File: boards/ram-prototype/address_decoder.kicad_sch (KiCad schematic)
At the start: 33 parts, among them U1 74LVC1G04, U10 74LVC1G11, U11 74LVC1G11, U2 74LVC1G04, U3 74LVC1G04, U4 74LVC1G11, U5 74LVC1G11, U6 74LVC1G11, U7 74LVC1G11, U8 74LVC1G11, U9 74LVC1G11

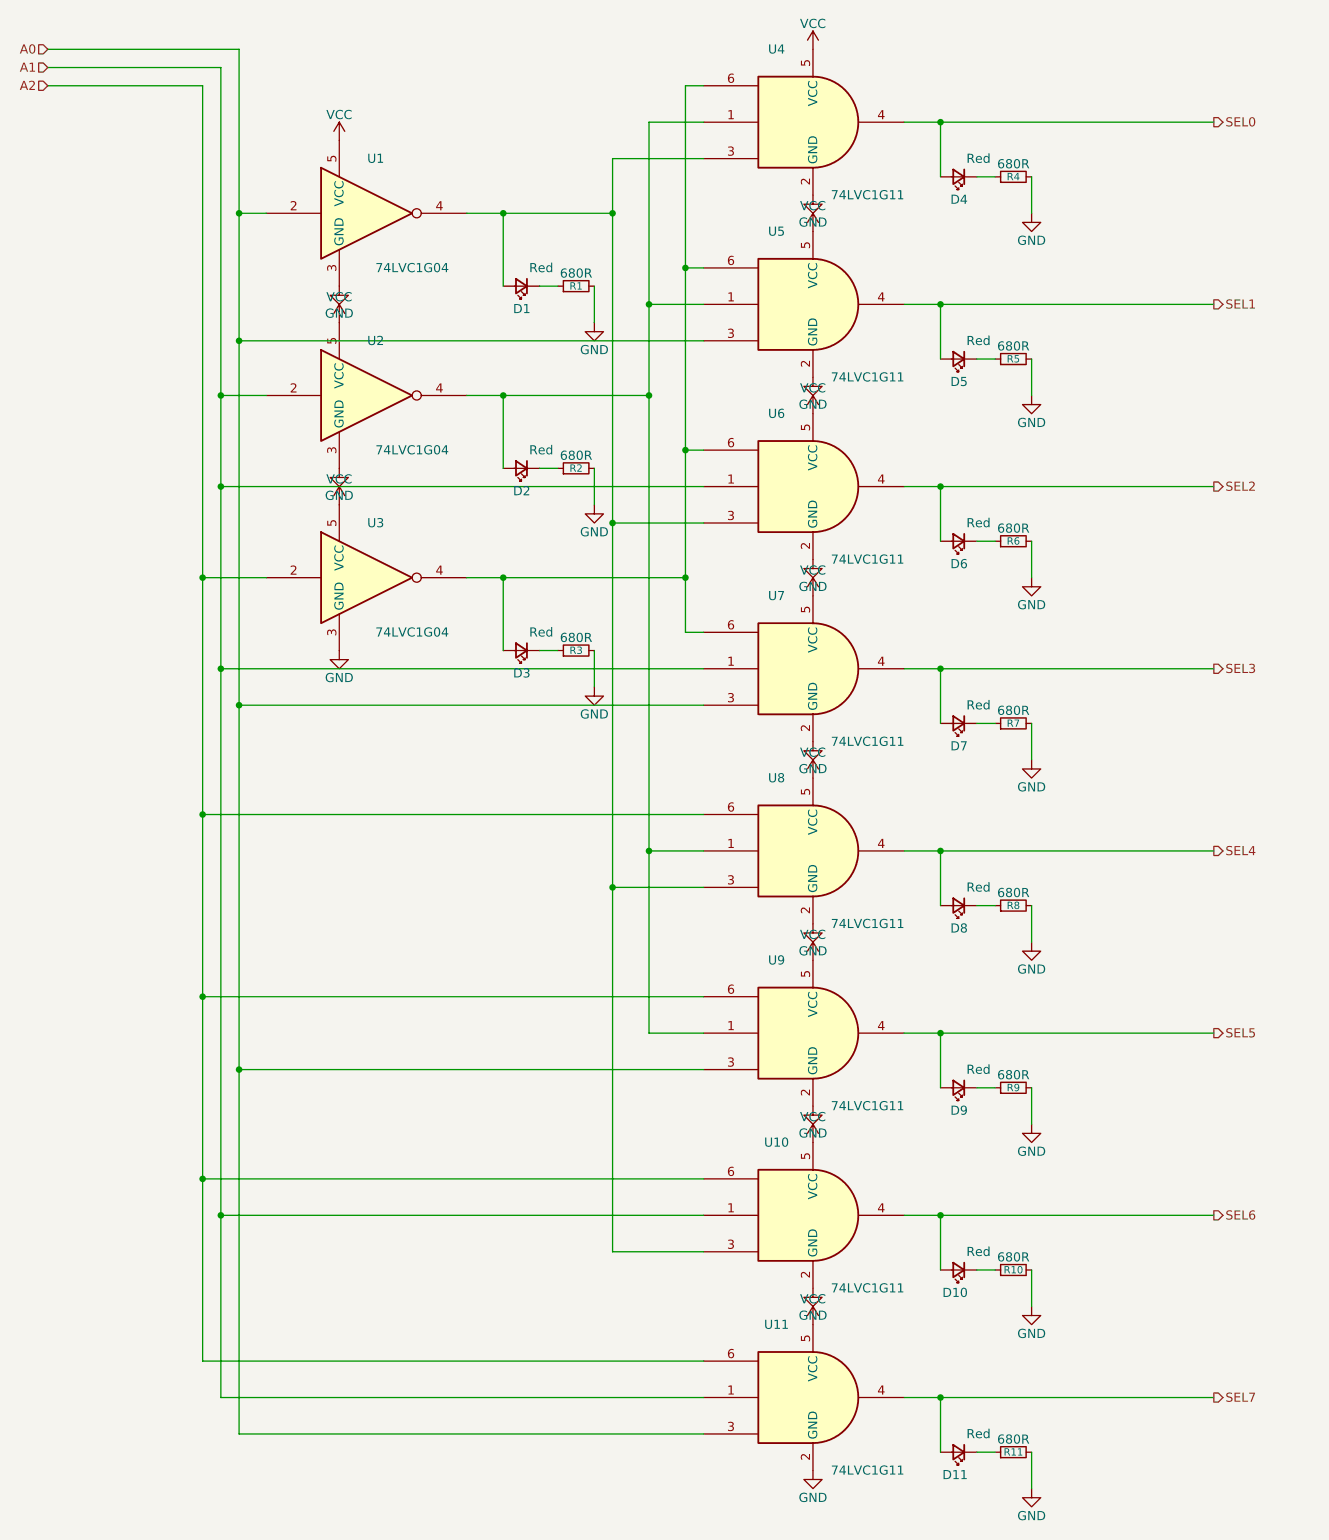
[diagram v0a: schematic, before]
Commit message: Update schematic with new row/col architecture
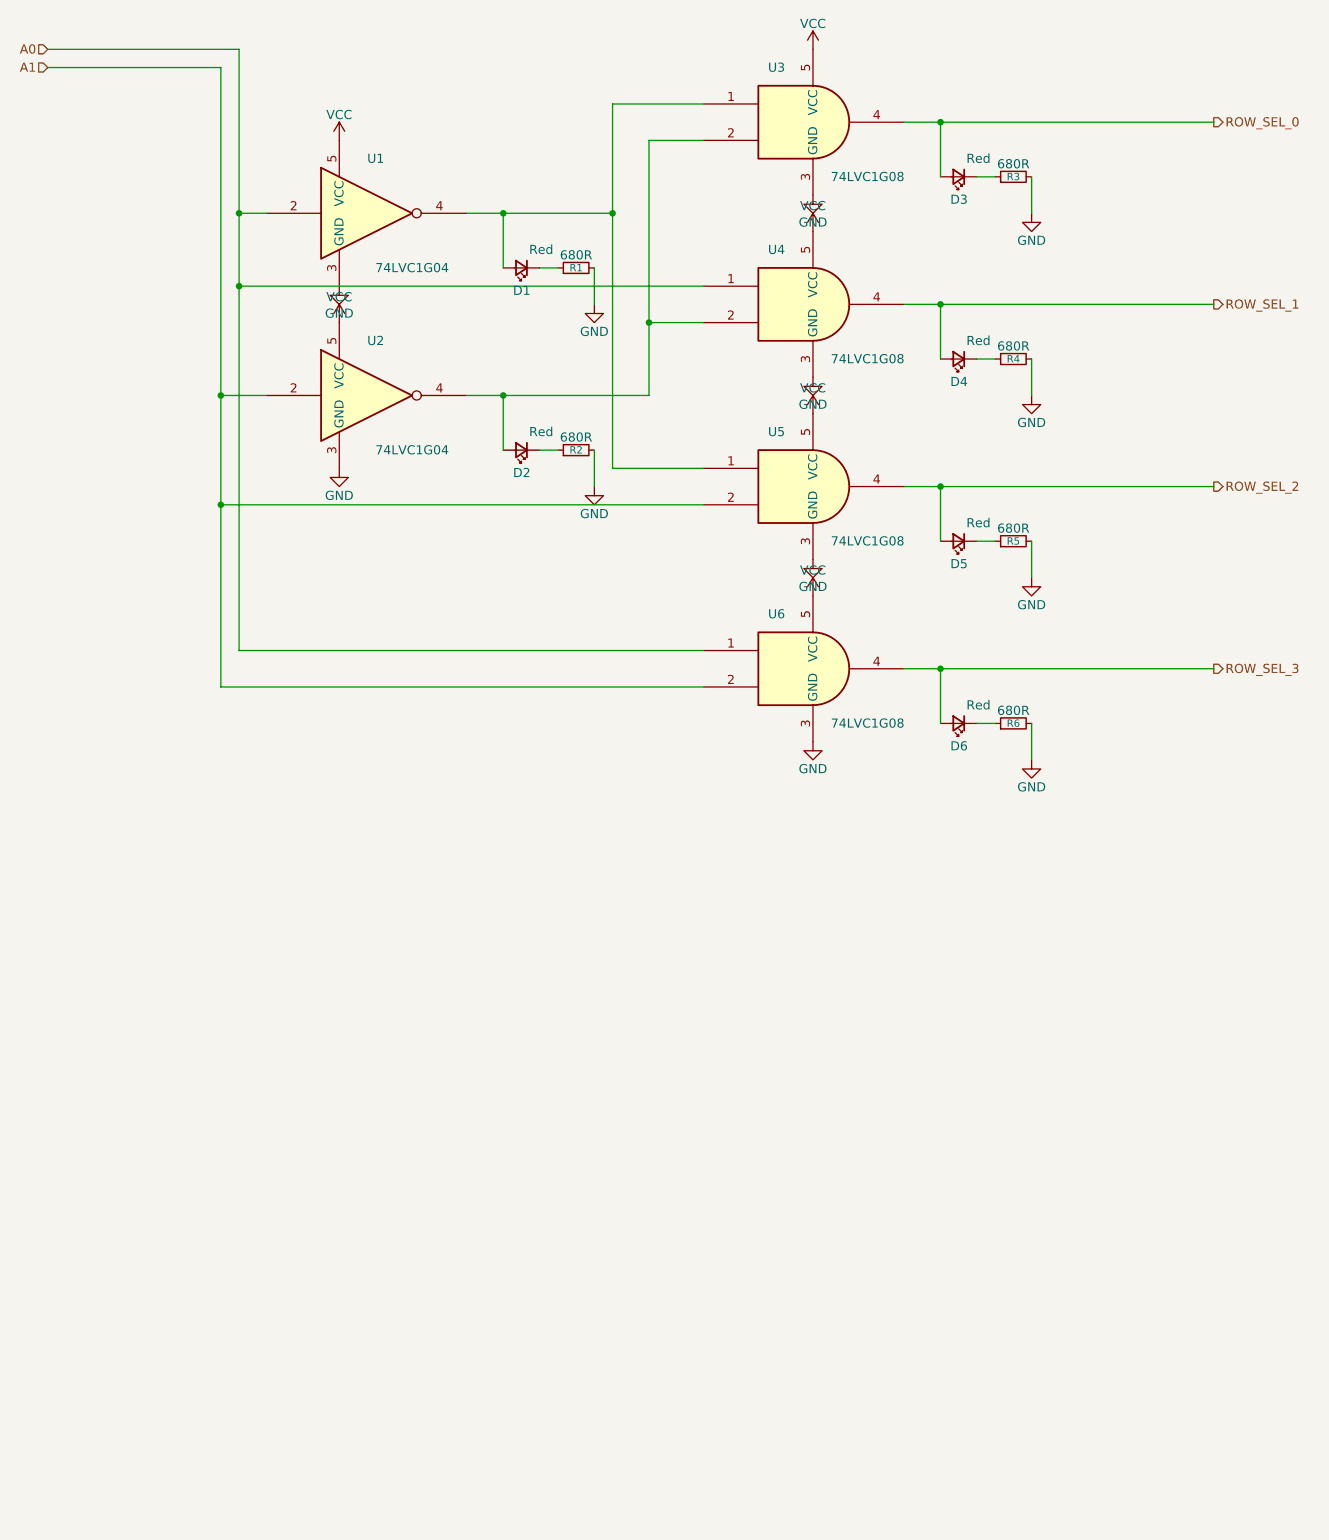
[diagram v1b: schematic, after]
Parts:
- removed D10, D11, D7, D8, D9: Red, symbol Device:LED_Small
- removed R10, R11, R7, R8, R9: 680R, symbol Device:R_Small
- removed U10, U11, U4, U5, U6, U7, U8, U9: 74LVC1G11, symbol 74xGxx:74LVC1G11
- removed U3: 74LVC1G04, symbol 74xGxx:74LVC1G04
- added U3, U4, U5, U6: 74LVC1G08, symbol 74xGxx:74LVC1G08
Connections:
- net A0: now also U4.1, U6.1
- net A1: now also U5.2, U6.2
- net GND: now also U3.3 (GND), U4.3 (GND), U5.3 (GND), U6.3 (GND)
- net VCC: now also U3.5 (VCC), U4.5 (VCC), U5.5 (VCC), U6.5 (VCC)
- net at D2.2 (A), U2.4: now also U3.2, U4.2
- net at D1.2 (A), U1.4: now also U3.1, U5.1
- net ROW_SEL_0: now reaches D3.2 (A)
- net ROW_SEL_0: now also U3.4
- net SEL0 renamed ROW_SEL_1
- net ROW_SEL_1: now also U4.4
- net SEL1 renamed ROW_SEL_2
- net ROW_SEL_2: now also U5.4
- net SEL2 renamed ROW_SEL_3
- net ROW_SEL_3: now also U6.4

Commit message: Add initial changes to make logic close to final
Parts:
- removed U3, U4, U5, U6: 74LVC1G08, symbol 74xGxx:74LVC1G08
- added D10, D11, D12, D13, D14, D15, D16, D17, D18, D19, D7, D8, D9: Red, symbol Device:LED_Small
- added R10, R11, R12, R13, R14, R15, R16, R17, R18, R19, R7, R8, R9: 680R, symbol Device:R_Small
- added U10, U11, U12, U13, U14, U15, U16, U17, U18, U19, U8, U9: 74LVC1G08, symbol 74xGxx:74LVC1G08
- added U3, U4, U5, U6, U7: 74LVC1G04, symbol 74xGxx:74LVC1G04
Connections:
- net A0: now also U13.2, U15.2
- net A1: now also U14.1, U15.1
- net GND: now also R10.2, R11.2, R12.2, R13.2, R14.2, R15.2, R16.2, R17.2, R18.2, R19.2, R7.2, R8.2, R9.2, U10.3 (GND), U11.3 (GND), U12.3 (GND), U13.3 (GND), U14.3 (GND), U15.3 (GND), U16.3 (GND), U17.3 (GND), U18.3 (GND), U19.3 (GND), U3.3 (GND), U4.3 (GND), U5.3 (GND), U6.3 (GND), U7.3 (GND), U8.3 (GND), U9.3 (GND)
- net ROW_SEL_0: now also D16.2 (A), U16.4; no longer D3.2 (A)
- net ROW_SEL_1: now also D17.2 (A), U17.4; no longer D4.2 (A)
- net ROW_SEL_2: now also D18.2 (A), U18.4; no longer D5.2 (A)
- net ROW_SEL_3: now also D19.2 (A), U19.4; no longer D6.2 (A)
- net VCC: now also U10.5 (VCC), U11.5 (VCC), U12.5 (VCC), U13.5 (VCC), U14.5 (VCC), U15.5 (VCC), U16.5 (VCC), U17.5 (VCC), U18.5 (VCC), U19.5 (VCC), U3.5 (VCC), U4.5 (VCC), U5.5 (VCC), U6.5 (VCC), U7.5 (VCC), U8.5 (VCC), U9.5 (VCC)
- net at D1.2 (A), U1.4: now also U12.2, U14.2
- net at D2.2 (A), U2.4: now also U12.1, U13.1
- new net: D9.1 (K), R9.1
- new net: D15.1 (K), R15.1
- new net: D15.2 (A), U15.4, U19.2
- new net: D10.1 (K), R10.1
- new net: D7.1 (K), R7.1
- new net: D14.2 (A), U14.4, U18.2
- new net: D6.2 (A), U6.4, U9.2
- new net: D18.1 (K), R18.1
- new net: D12.2 (A), U12.4, U16.2
- new net: D7.2 (A), U11.2, U7.4
- new net: D4.2 (A), U4.4, U8.2
- new net: D14.1 (K), R14.1
- new net: D8.1 (K), R8.1
- new net: D5.2 (A), U5.4, U9.1
- new net: D16.1 (K), R16.1
- new net: D12.1 (K), R12.1
- new net: D13.1 (K), R13.1
- new net: D13.2 (A), U13.4, U17.2
- new net: D19.1 (K), R19.1
- new net: D11.1 (K), R11.1
- new net: D3.2 (A), U3.4, U8.1
- new net: D17.1 (K), R17.1
- new net A2: U3.2
- new net A3: U4.2
- new net A4: U5.2
- new net A5: U6.2
- new net A6: U7.2
- new net RS1: D8.2 (A), U10.1, U8.4
- new net RS2: D9.2 (A), U10.2, U9.4
- new net RS3: D10.2 (A), U10.4, U11.1
- new net RS4: D11.2 (A), U11.4, U16.1, U17.1, U18.1, U19.1

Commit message: Update row select to have the full complexity to test latency
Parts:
- added D20, D21, D22, D23, D24, D25, D26, D27, D28, D29, D30, D31, D32, D33, D34, D35, D36, D37, D38, D39, D40, D41, D42, D43, D44, D45, D46, D47: Red, symbol Device:LED_Small
- added R20, R21, R22, R23, R24, R25, R26, R27, R28, R29, R30, R31, R32, R33, R34, R35, R36, R37, R38, R39, R40, R41, R42, R43, R44, R45, R46, R47: 680R, symbol Device:R_Small
- added U20, U21, U22, U23, U24, U25, U26, U27, U28, U29, U30, U31, U32, U33, U34, U35, U36, U37, U38, U39, U40, U41, U42, U43, U44, U45, U46, U47: 74LVC1G08, symbol 74xGxx:74LVC1G08
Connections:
- net A0: now also U17.2, U19.2
- net A1: now also U11.2, U9.2; no longer U14.1, U15.1
- net A2: now also U10.1, U11.1
- net A3: now also U21.2, U23.2
- net A4: now also U22.1, U23.1
- net A5: now also U25.2, U27.2
- net A6: now also U26.1, U27.1
- net GND: now also R20.2, R21.2, R22.2, R23.2, R24.2, R25.2, R26.2, R27.2, R28.2, R29.2, R30.2, R31.2, R32.2, R33.2, R34.2, R35.2, R36.2, R37.2, R38.2, R39.2, R40.2, R41.2, R42.2, R43.2, R44.2, R45.2, R46.2, R47.2, U20.3 (GND), U21.3 (GND), U22.3 (GND), U23.3 (GND), U24.3 (GND), U25.3 (GND), U26.3 (GND), U27.3 (GND), U28.3 (GND), U29.3 (GND), U30.3 (GND), U31.3 (GND), U32.3 (GND), U33.3 (GND), U34.3 (GND), U35.3 (GND), U36.3 (GND), U37.3 (GND), U38.3 (GND), U39.3 (GND), U40.3 (GND), U41.3 (GND), U42.3 (GND), U43.3 (GND), U44.3 (GND), U45.3 (GND), U46.3 (GND), U47.3 (GND)
- net ROW_SEL_0: now also D44.2 (A), U44.4; no longer D16.2 (A), U16.4
- net ROW_SEL_1: now also D45.2 (A), U45.4; no longer D17.2 (A), U17.4
- net ROW_SEL_2: now also D46.2 (A), U46.4; no longer D18.2 (A), U18.4
- net ROW_SEL_3: now also D47.2 (A), U47.4; no longer D19.2 (A), U19.4
- net VCC: now also U20.5 (VCC), U21.5 (VCC), U22.5 (VCC), U23.5 (VCC), U24.5 (VCC), U25.5 (VCC), U26.5 (VCC), U27.5 (VCC), U28.5 (VCC), U29.5 (VCC), U30.5 (VCC), U31.5 (VCC), U32.5 (VCC), U33.5 (VCC), U34.5 (VCC), U35.5 (VCC), U36.5 (VCC), U37.5 (VCC), U38.5 (VCC), U39.5 (VCC), U40.5 (VCC), U41.5 (VCC), U42.5 (VCC), U43.5 (VCC), U44.5 (VCC), U45.5 (VCC), U46.5 (VCC), U47.5 (VCC)
- net nA3: now reaches D4.2 (A), U4.4
- net nA3: now also U20.2, U22.2; no longer U8.2
- net nA2: now reaches D3.2 (A), U3.4, U8.1
- net nA2: now also U9.1
- net G0: now reaches U12.1, U13.1
- net G0: now also D8.2 (A), U8.4; no longer D2.2 (A), U2.4
- net nA0: now reaches D1.2 (A), U1.4, U12.2, U14.2
- net nA0: now also U16.2, U18.2
- net DEC3_0: now reaches D12.2 (A), U12.4
- net DEC3_0: now also U44.1; no longer U16.2
- net nA4: now reaches D5.2 (A), U5.4
- net nA4: now also U20.1, U21.1; no longer U9.1
- net nA5: now reaches D6.2 (A), U6.4
- net nA5: now also U24.2, U26.2; no longer U9.2
- net DEC3_1: now reaches D13.2 (A), U13.4
- net DEC3_1: now also U45.1; no longer U17.2
- net DEC3_2: now reaches D14.2 (A), U14.4
- net DEC3_2: now also U46.1; no longer U18.2
- net nA6: now reaches D7.2 (A), U7.4
- net nA6: now also U24.1, U25.1; no longer U11.2
- net DEC3_3: now reaches D15.2 (A), U15.4
- net DEC3_3: now also U47.1; no longer U19.2
- removed net RS1: D8.2 (A), U10.1, U8.4
- net RS2 renamed G1
- net G1: now also U14.1, U15.1; no longer U10.2
- net RS3 renamed G2
- net G2: now also U16.1, U17.1; no longer U11.1
- net RS4 renamed G3
- net G3: no longer U16.1, U17.1
- new net: D24.1 (K), R24.1
- new net: D47.1 (K), R47.1
- new net: D33.1 (K), R33.1
- new net: D32.1 (K), R32.1
- new net: D44.1 (K), R44.1
- new net: D37.1 (K), R37.1
- new net: D29.1 (K), R29.1
- new net: D23.1 (K), R23.1
- new net: D26.1 (K), R26.1
- new net: D38.1 (K), R38.1
- new net: D45.1 (K), R45.1
- new net: D35.1 (K), R35.1
- new net: D39.1 (K), R39.1
- new net: D21.1 (K), R21.1
- new net: D27.1 (K), R27.1
- new net: D46.1 (K), R46.1
- new net: D42.1 (K), R42.1
- new net: D43.1 (K), R43.1
- new net: D36.1 (K), R36.1
- new net: D30.1 (K), R30.1
- new net: D41.1 (K), R41.1
- new net: D28.1 (K), R28.1
- new net: D20.1 (K), R20.1
- new net: D34.1 (K), R34.1
- new net: D22.1 (K), R22.1
- new net: D31.1 (K), R31.1
- new net: D25.1 (K), R25.1
- new net: D40.1 (K), R40.1
- new net DEC3_4: D16.2 (A), U16.4
- new net DEC3_5: D17.2 (A), U17.4
- new net DEC3_6: D18.2 (A), U18.4
- new net DEC3_7: D19.2 (A), U19.4
- new net DEC4_0: D28.2 (A), U28.4, U44.2, U45.2, U46.2, U47.2
- new net DEC4_1: D29.2 (A), U29.4
- new net DEC4_10: D38.2 (A), U38.4
- new net DEC4_11: D39.2 (A), U39.4
- new net DEC4_12: D40.2 (A), U40.4
- new net DEC4_13: D41.2 (A), U41.4
- new net DEC4_14: D42.2 (A), U42.4
- new net DEC4_15: D43.2 (A), U43.4
- new net DEC4_2: D30.2 (A), U30.4
- new net DEC4_3: D31.2 (A), U31.4
- new net DEC4_4: D32.2 (A), U32.4
- new net DEC4_5: D33.2 (A), U33.4
- new net DEC4_6: D34.2 (A), U34.4
- new net DEC4_7: D35.2 (A), U35.4
- new net DEC4_8: D36.2 (A), U36.4
- new net DEC4_9: D37.2 (A), U37.4
- new net HA0: D20.2 (A), U20.4, U28.2, U32.2, U36.2, U40.2
- new net HA1: D21.2 (A), U21.4, U29.2, U33.2, U37.2, U41.2
- new net HA2: D22.2 (A), U22.4, U30.2, U34.2, U38.2, U42.2
- new net HA3: D23.2 (A), U23.4, U31.2, U35.2, U39.2, U43.2
- new net HB0: D24.2 (A), U24.4, U28.1, U29.1, U30.1, U31.1
- new net HB1: D25.2 (A), U25.4, U32.1, U33.1, U34.1, U35.1
- new net HB2: D26.2 (A), U26.4, U36.1, U37.1, U38.1, U39.1
- new net HB3: D27.2 (A), U27.4, U40.1, U41.1, U42.1, U43.1
- new net nA1: D2.2 (A), U10.2, U2.4, U8.2

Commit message: Fix a bunch of issues
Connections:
- net A0: now also U7.2; no longer U1.2
- net A1: now also U6.2; no longer U2.2
- net A2: now also U5.2; no longer U3.2
- net A4: now also U3.2; no longer U5.2
- net A5: now also U2.2; no longer U6.2
- net A6: now also U1.2; no longer U7.2
- net nA0: now also D7.2 (A), U7.4; no longer D1.2 (A), U1.4
- net nA1: now also D6.2 (A), U6.4; no longer D2.2 (A), U2.4
- net nA2: now also D5.2 (A), U5.4; no longer D3.2 (A), U3.4
- net nA4: now also D3.2 (A), U3.4; no longer D5.2 (A), U5.4
- net nA5: now also D2.2 (A), U2.4; no longer D6.2 (A), U6.4
- net nA6: now also D1.2 (A), U1.4; no longer D7.2 (A), U7.4
